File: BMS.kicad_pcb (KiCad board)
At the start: 4 copper layers, 44 x 71 mm, 129 parts, among them J1 12402012E212A, J3 Conn_01x02_Socket, J4 Conn_01x03_Pin, J5 Conn_01x10_Pin, J6 Conn_01x02_Pin, Q1 FZT853TA, Q2 PSMN020-100YS, Q3 PSMN020-100YS, Q4 PSMN3R7-100BSE, Q5 PSMN3R7-100BSE, SW1 SW_Push, SW2 SW_Push, U1 USBLC6-2SC6, U10 SQ1464EEH-T1_GE3, U11 MP2790DFP-0000-T, U12 TPS7B8133QDGNRQ1, U2 USBLC6-2SC6, U3 RP2350A, U5 SQ1464EEH-T1_GE3, U6 SQ1464EEH-T1_GE3, U7 SQ1464EEH-T1_GE3, U8 SQ1464EEH-T1_GE3, U9 SQ1464EEH-T1_GE3, X1 ABM8-272-T3

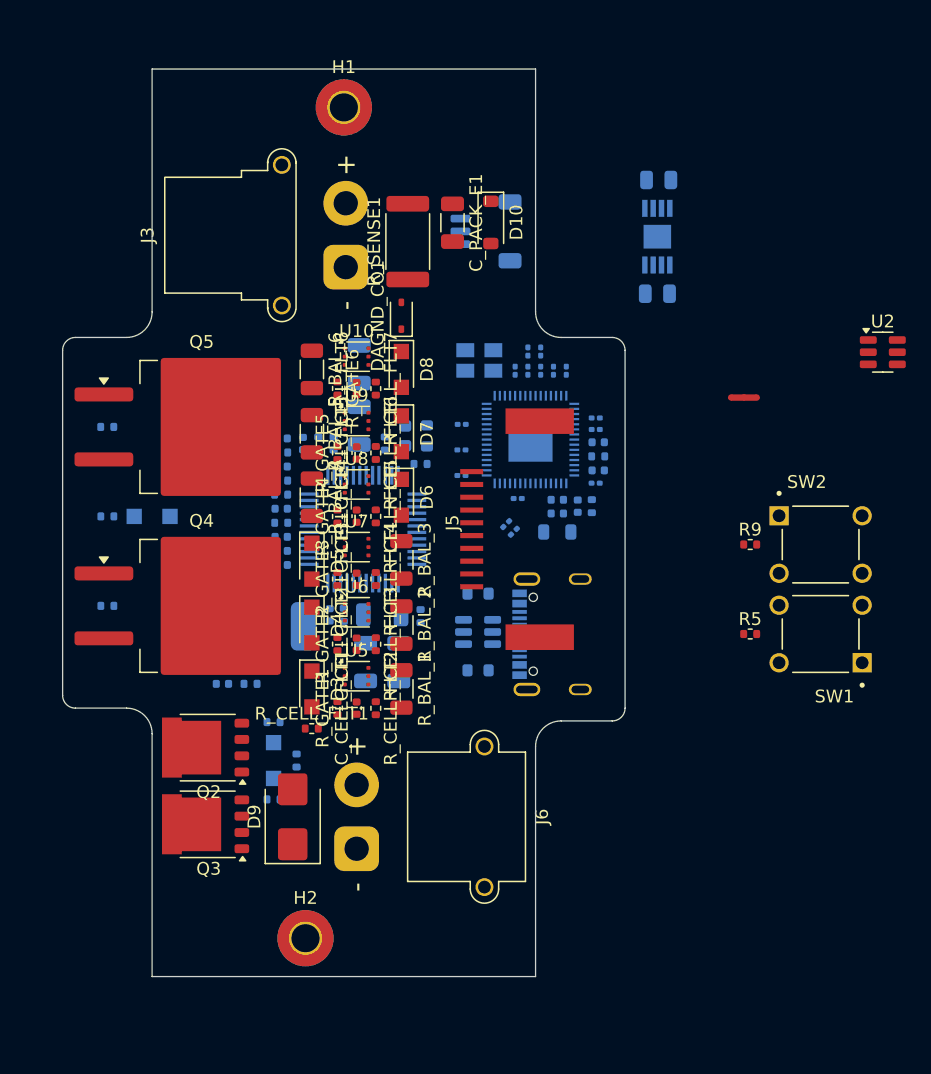
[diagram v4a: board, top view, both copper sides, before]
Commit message: Adding proper grounding
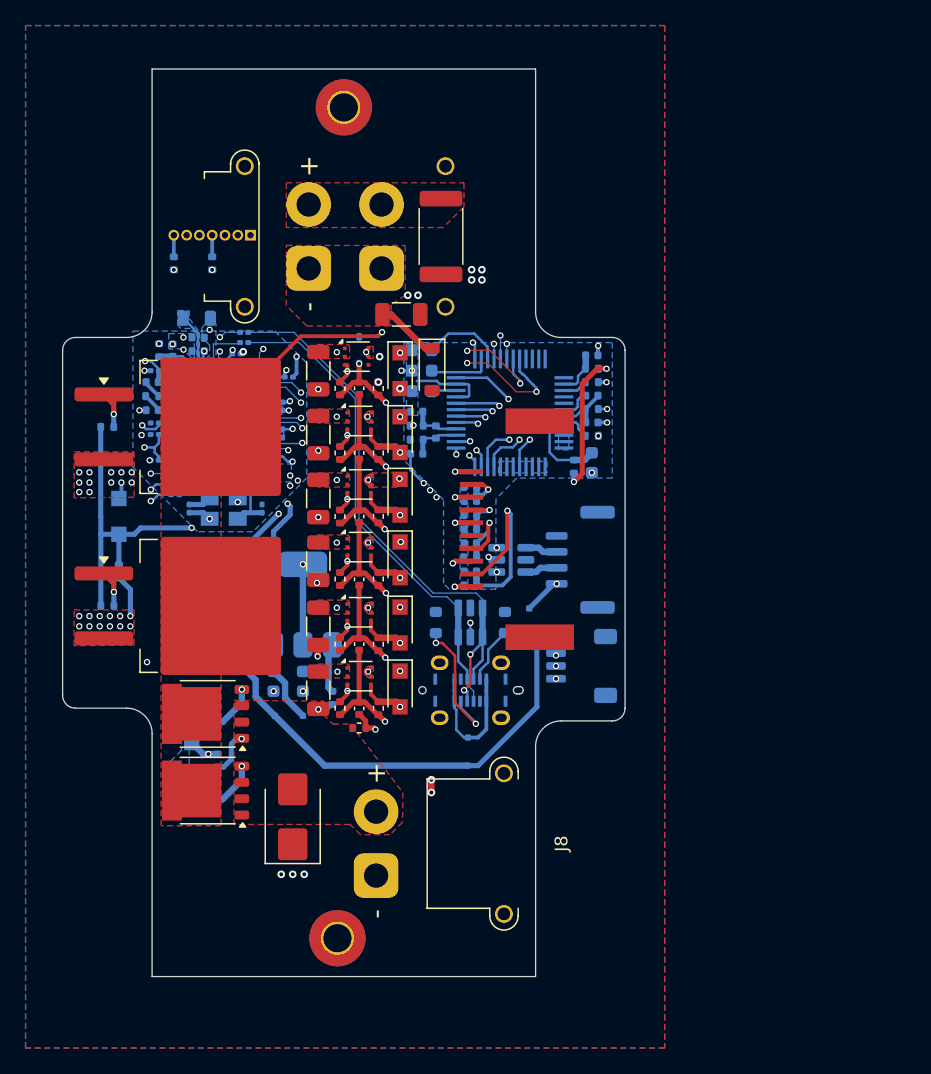
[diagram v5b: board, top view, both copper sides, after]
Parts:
- removed C4: 100n, Capacitor_SMD:C_0201_0603Metric
- removed C_3V1: 1 μF, Capacitor_SMD:C_0402_1005Metric
- removed the J4 at (161.0, 76.1)
- removed SW1, SW2: SW_Push, _BMS:SW_TS02-66-43-BK-160-LCR-D
- added C_3V3_1: 1 μF, Capacitor_SMD:C_0603_1608Metric, B.Cu at (156.0, 87.0)
- added D1: SS16HE, Diode_SMD:D_SOD-323F, B.Cu at (164.4, 106.7)
- added D11: SS16HE, Diode_SMD:D_SOD-323F, B.Cu at (159.6, 116.8)
- added D2: SS16HE, Diode_SMD:D_SOD-323F, B.Cu at (145.6, 114.0)
- added J2: Conn_01x04_Socket, Connector_JST:JST_GH_SM04B-GHS-TB_1x04-1MP_P1.25mm_Horizontal, B.Cu at (168.4, 101.8)
- added J3: Conn_01x02_Socket, Connector_AMASS:AMASS_XT30PW-F_1x02_P2.50mm_Horizontal, B.Cu at (152.8, 79.0)
- added J5: Conn_01x07_Socket, Connector_PinHeader_1.00mm:PinHeader_1x07_P1.00mm_Vertical, B.Cu at (142.6, 76.4)
- added J6: Conn_01x03_Pin, Connector_JST:JST_SH_SM03B-SRSS-TB_1x03-1MP_P1.00mm_Horizontal, B.Cu at (168.5, 110.1)
- C_CP1, C_MID1, C_SRN_GND1, C_SRN_SRP1, C_SRP_GND1: footprint Capacitor_SMD:C_1206_3216Metric -> Capacitor_SMD:C_0402_1005Metric
- C_REG1, C_VDD1, C_VREF1: footprint Capacitor_SMD:C_0402_1005Metric -> Capacitor_SMD:C_0603_1608Metric
- DAGND_CO1, R5, U2: moved to B.Cu
- J1: value 12402012E212A -> GSB1CA11101DSHR; footprint _BMS:AMPHENOL_12402012E212A -> _BMS:AMPHENOL_GSB1CA11101DSHR
- NT1: footprint NetTie:NetTie-3_SMD_Pad0.5mm -> NetTie:NetTie-2_SMD_Pad0.5mm
- R7: renamed from R9; moved to B.Cu
- R_MID1: footprint Resistor_SMD:R_0603_1608Metric -> Resistor_SMD:R_0402_1005Metric
- moved R5 53.6 mm to (136.6, 78.6), turned to -90 degrees
- moved C16 50.7 mm to (140.4, 109.6)
- moved R7 47.5 mm to (139.6, 78.6), turned to 90 degrees
- moved U4 44.5 mm to (140.6, 105.3), turned to 90 degrees
- moved C17 39.4 mm to (140.6, 101.0)
- moved NT1 39.0 mm to (156.8, 119.5), turned to 90 degrees
- moved R12 36.0 mm to (135.4, 85.4), turned to -90 degrees
- moved C10 35.6 mm to (135.1, 87.0), turned to 180 degrees
- moved R8 35.6 mm to (134.9, 87.9), turned to 180 degrees
- moved R9 35.2 mm to (134.9, 89.0), turned to 180 degrees
- moved C11 35.0 mm to (134.9, 90.1), turned to 180 degrees
- moved C12 34.5 mm to (135.1, 92.0), turned to 180 degrees
- moved C9 34.5 mm to (135.1, 91.1), turned to 180 degrees
- moved C13 34.0 mm to (136.5, 85.4), turned to 90 degrees
- moved U2 33.3 mm to (163.0, 101.8), turned to 180 degrees
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- renumbered C9 to C10, C22 to C16, C23 to C17, C10 to C9, J3 to J4, J5 to J7, J6 to J8, R7 to R8, R8 to R9, U12 to U4
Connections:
- net /main/microcontroller/SWCLK renamed /main/microcontroller/SWCLK_INT
- net /main/microcontroller/SWDIO renamed /main/microcontroller/SWDIO_INT
- C1 pad 1: GND -> GNDREF
- C10 pad 2: GND -> GNDREF
- C11 pad 2: GND -> GNDREF
- C12 pad 2: GND -> GNDREF
- C13 pad 2: GND -> GNDREF
- C14 pad 1: GND -> GNDREF
- C15 pad 1: GND -> GNDREF
- C2 pad 1: GND -> GNDREF
- C3 pad 1: GND -> GNDREF
- C5 pad 1: GND -> GNDREF
- C6 pad 2: GND -> GNDREF
- C7 pad 2: GND -> GNDREF
- C8 pad 2: GND -> GNDREF
- C9 pad 2: GND -> GNDREF
- C_REG1 pad 2: GNDREF -> GND
- C_SRN_GND1 pad 1: GNDREF -> /main/BMS/SRN
- C_SRN_GND1 pad 2: /main/BMS/SRN -> GNDREF
- C_SRP_GND1 pad 1: /main/BMS/SRP -> GNDREF
- C_SRP_GND1 pad 2: GNDREF -> /main/BMS/SRP
- C_VREF1 pad 1: GNDREF -> Net-(U11-VREF)
- C_VREF1 pad 2: Net-(U11-VREF) -> GNDREF
- J1 pad A6: Net-(J1-D+_A) -> /main/external_io/D+
- J1 pad A7: Net-(J1-D-_A) -> /main/external_io/D-
- R3 pad 1: Net-(J4-Pin_1) -> /main/external_io/SWCLK
- R4 pad 2: Net-(J4-Pin_3) -> /main/external_io/SWDIO
- R5 pad 1: GND -> /main/external_io/RUN
- R5 pad 2: Net-(R5-Pad2) -> Net-(U3-RUN)
- R7 pad 1: Net-(R9-Pad1) -> /main/microcontroller/QSPI_SS
- R7 pad 2: GND -> /main/external_io/BOOT
- R_MID1 pad 1: Net-(U11-VMID) -> /main/BMS/DRAIN
- R_MID1 pad 2: /main/BMS/DRAIN -> Net-(U11-VMID)
- U1 pad 1: Net-(J1-D+_A) -> /main/external_io/D+
- U1 pad 3: Net-(J1-D-_A) -> /main/external_io/D-
- U3 pad 10: unconnected-(U3-GPIO7-Pad10) -> /main/BMS/SCL
- U3 pad 12: unconnected-(U3-GPIO8-Pad12) -> GNDREF
- U3 pad 13: unconnected-(U3-GPIO9-Pad13) -> GNDREF
- U3 pad 17: unconnected-(U3-GPIO13-Pad17) -> GNDREF
- U3 pad 18: unconnected-(U3-GPIO14-Pad18) -> GNDREF
- U3 pad 19: unconnected-(U3-GPIO15-Pad19) -> GNDREF
- U3 pad 2: /main/BMS/SDA -> /main/external_io/TX
- U3 pad 20: unconnected-(U3-IOVDD-Pad20) -> GNDREF
- U3 pad 3: /main/BMS/SCL -> /main/external_io/RX
- U3 pad 47: GND -> GNDREF
- U3 pad 60: Net-(U3-QSPI_SS) -> /main/microcontroller/QSPI_SS
- U3 pad 61: GND -> GNDREF
- U3 pad 7: unconnected-(U3-GPIO4-Pad7) -> GNDREF
- U3 pad 8: unconnected-(U3-GPIO5-Pad8) -> GNDREF
- U3 pad 9: unconnected-(U3-GPIO6-Pad9) -> /main/BMS/SDA
- X1 pad 2: GND -> GNDREF
- X1 pad 4: GND -> GNDREF
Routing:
- net +3V3: track 0.00 -> 75.3 mm, vias 0 -> 8
- net Net-(D_CHG_VGS2-K): track 0.00 -> 62.3 mm, vias 0 -> 2
- net /main/BMS/TOP: track 0.00 -> 54.0 mm, vias 0 -> 4
- net Net-(D_CHG_VGS1-K): track 0.00 -> 50.2 mm, vias 0 -> 2
- net /main/BMS/SCL: track 0.00 -> 47.4 mm, vias 0 -> 4
- net /main/INT_5V: track 0.00 -> 45.9 mm, vias 0 -> 2
- net +1V1: track 0.00 -> 45.5 mm, vias 0 -> 3
- net /main/external_io/D+: track 0.00 -> 44.9 mm, vias 0 -> 2
- net /main/BMS/SDA: track 0.00 -> 42.9 mm, vias 0 -> 4
- net /main/external_io/SWCLK: track 0.00 -> 40.2 mm, vias 0 -> 2
- net /main/external_io/SWDIO: track 0.00 -> 40.1 mm, vias 0 -> 2
- net /main/BMS/CELL_5: track 0.00 -> 39.9 mm, vias 0 -> 2
- net /main/external_io/D-: track 0.00 -> 38.4 mm
- net /main/BMS/DRAIN: track 0.00 -> 37.4 mm, vias 0 -> 2
- net /main/housekeeping/5V_IN: track 0.00 -> 35.5 mm
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- added copper zone on B.Cu, net +1V1
- added copper zone on B.Cu, net /main/BMS/C10
- added copper zone on B.Cu, net /main/BMS/CELL_6
- added copper zone on F.Cu, net /main/BMS/DRAIN
- added copper zone on F.Cu, net /main/BMS/PACK+
- added copper zone on In1.Cu, net /main/BMS/PACK+
- added copper zone on F.Cu, net /main/BMS/PACK-
- added copper zone on F.Cu, net /main/BMS/TOP
- added copper zone on B.Cu, net /main/housekeeping/5V_IN
- added copper zone on B.Cu, net GND
- added copper zone on F.Cu, net GND
- added copper zone on In1.Cu, net GND
- added copper zone on In2.Cu, net GND
- added copper zone on In3.Cu, net GND
- added copper zone on In4.Cu, net GND
- added copper zone on B.Cu, net GNDREF
- added copper zone on In4.Cu, net GNDREF
- added copper zone on B.Cu, net Net-(D_CHG_VGS1-K)
- added copper zone on F.Cu, net Net-(R_BAL_1-Pad1)
- added copper zone on F.Cu, net Net-(R_BAL_2-Pad1)
- added copper zone on F.Cu, net Net-(R_BAL_3-Pad1)
- added copper zone on F.Cu, net Net-(R_BAL_4-Pad1)
- added copper zone on F.Cu, net Net-(R_BAL_5-Pad1)
- added copper zone on F.Cu, net Net-(R_BAL_6-Pad1)
- added copper zone on B.Cu, net Net-(U3-VREG_LX)
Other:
- copper layers 4 -> 6
- board text added: "-"

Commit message: Lots of changfes
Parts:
- removed the C20 at (159.8, 100.5)
- removed the J1 at (159.8, 112.0)
- removed NT1: NetTie_2, NetTie:NetTie-2_SMD_Pad0.5mm
- removed the R8 at (134.9, 87.9)
- removed the R9 at (134.9, 89.0)
- added C0: CELL0, _BMS:Harwin TP, F.Cu at (156.7, 87.4)
- added C1: CELL1, _BMS:Harwin TP, F.Cu at (156.4, 93.5)
- added C2: CELL2, _BMS:Harwin TP, F.Cu at (156.5, 98.4)
- added C22: 10n, Capacitor_SMD:C_0402_1005Metric, B.Cu at (159.8, 100.4)
- added C23: 10n, Capacitor_SMD:C_0402_1005Metric, B.Cu at (159.8, 102.7)
- added C3: CELL3, _BMS:Harwin TP, F.Cu at (156.5, 103.4)
- added C4: CELL4, _BMS:Harwin TP, F.Cu at (156.5, 108.4)
- added C4: 100n, Capacitor_SMD:C_0201_0603Metric, B.Cu at (144.2, 95.6)
- added C5: CELL5, _BMS:Harwin TP, F.Cu at (156.5, 110.9)
- added C5: 100n, Capacitor_SMD:C_0201_0603Metric, B.Cu at (138.8, 95.6)
- added C6: CELL6, _BMS:Harwin TP, F.Cu at (156.5, 114.1)
- added G***: LOGO, LOGO, F.Cu at (157.2, 131.5)
- added J6: 2169890001, _BMS:216989-0001_MOL, F.Cu at (138.6, 124.9)
- added R5: R, Resistor_SMD:R_0402_1005Metric, B.Cu at (163.6, 82.6)
- added R6: R, Resistor_SMD:R_0402_1005Metric, B.Cu at (162.5, 82.6)
- R_MID1, R_PACK_FLT1, R_TOP_FLT1: footprint Resistor_SMD:R_0402_1005Metric -> Resistor_SMD:R_0603_1608Metric
- R_REG1: footprint Resistor_SMD:R_0402_1005Metric -> Resistor_SMD:R_1206_3216Metric
- moved R2 29.3 mm to (142.9, 128.5), turned to 180 degrees
- moved R1 23.7 mm to (139.2, 122.2), turned to 0 degrees
- moved D1 21.9 mm to (145.6, 118.0), turned to 0 degrees
- moved U1 19.9 mm to (145.6, 120.7), turned to 180 degrees
- moved D3 14.0 mm to (145.6, 116.0), turned to 0 degrees
- moved C19 10.9 mm to (156.3, 89.1)
- moved D11 10.4 mm to (155.9, 76.5), turned to 90 degrees
- moved C_PACK_E1 7.24 mm to (158.3, 76.5), turned to 90 degrees
- moved R_SENSE1 3.90 mm to (161.4, 76.5)
- moved C21 3.30 mm to (159.8, 99.4)
- moved D10 2.02 mm to (147.8, 122.6)
- moved C_PACK_FLT1 1.76 mm to (167.7, 86.4), turned to 180 degrees
- moved R11 1.17 mm to (141.5, 83.8)
- moved R9 1.00 mm to (140.6, 78.6)
- moved R_PACK_FLT1 0.96 mm to (170.1, 86.4)
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- renumbered C9 to C10, C10 to C11, C11 to C12, C12 to C13, C13 to C14, C14 to C15, C15 to C16, C16 to C17, C17 to C18, C18 to C20, C5 to C6, C6 to C7, C7 to C8, C8 to C9, D9 to D10, D10 to D11, D11 to D3, D3 to D4, D4 to D5, D5 to D6, D6 to D7, D7 to D8, D8 to D9, J2 to J1, J3 to J2, J4 to J3, J5 to J4, J6 to J5, R5 to R7, R6 to R8, R7 to R9
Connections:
- net Net-(U3-USB_DM) renamed /main/microcontroller/D-
- net Net-(U3-USB_DP) renamed /main/microcontroller/D+
- C1 pad 1: GNDREF -> GND
- C10 pad 2: GNDREF -> GND
- C11 pad 2: GNDREF -> GND
- C12 pad 1: Net-(C11-Pad1) -> +3V3
- C12 pad 2: GNDREF -> GND
- C13 pad 2: GNDREF -> GND
- C14 pad 2: GNDREF -> GND
- C15 pad 1: GNDREF -> GND
- C16 pad 1: GNDREF -> GND
- C19 pad 1: GNDREF -> GND
- C19 pad 2: /main/BMS/NTC3 -> Net-(U11-NTCB)
- C2 pad 1: GNDREF -> GND
- C20 pad 1: GNDREF -> GND
- C21 pad 1: GNDREF -> GND
- C21 pad 2: /main/BMS/NTC1 -> /main/BMS/NTC3
- C3 pad 1: GNDREF -> GND
- C6 pad 1: GNDREF -> GND
- C7 pad 2: GNDREF -> GND
- C8 pad 2: GNDREF -> GND
- C9 pad 2: GNDREF -> GND
- C_3V3_1 pad 1: GNDREF -> GND
- C_MID1 pad 2: GNDREF -> GND
- C_PACK_E1 pad 2: GND -> /main/BMS/PACK-
- C_PACK_FLT1 pad 2: GNDREF -> GND
- C_REGIN1 pad 1: GNDREF -> GND
- C_SRN_GND1 pad 2: GNDREF -> GND
- C_SRP_GND1 pad 1: GNDREF -> GND
- C_TOP_FLT1 pad 2: GNDREF -> GND
- C_VDD1 pad 2: GNDREF -> GND
- C_VREF1 pad 2: GNDREF -> GND
- D11 pad 2: GND -> /main/BMS/PACK-
- D3 pad 2: VBUS_A -> /main/V_USB
- J4 pad 3: GND -> /main/external_io/BOOT
- J4 pad 4: /main/external_io/BOOT -> GND
- J4 pad 5: GND -> /main/BMS/NSHDN
- R13 pad 2: GNDREF -> Net-(U11-NTCB)
- R14 pad 2: GNDREF -> Net-(U11-NTCB)
- R15 pad 2: GNDREF -> Net-(U11-NTCB)
- R16 pad 2: GNDREF -> Net-(U11-NTCB)
- R_PACK_FLT1 pad 2: /main/BMS/TOP -> /main/BMS/PACK+
- U11 pad 21: GNDREF -> Net-(U11-NTCB)
- U11 pad 23: GNDREF -> GND
- U3 pad 12: GNDREF -> GND
- U3 pad 13: GNDREF -> GND
- U3 pad 17: GNDREF -> GND
- U3 pad 18: GNDREF -> GND
- U3 pad 19: GNDREF -> GND
- U3 pad 20: GNDREF -> +3V3
- U3 pad 44: /main/microcontroller/ADC_VREF -> +3V3
- U3 pad 47: GNDREF -> GND
- U3 pad 61: GNDREF -> GND
- U3 pad 7: GNDREF -> GND
- U3 pad 8: GNDREF -> GND
- X1 pad 2: GNDREF -> GND
- X1 pad 4: GNDREF -> GND
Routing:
- net /main/BMS/NSHDN: track 27.0 -> 62.2 mm
- net /main/EXT_5V: track 10.7 -> 39.7 mm, vias 2 -> 3
- net /main/V_USB: track 0.00 -> 26.5 mm, vias 0 -> 1
- net /main/housekeeping/5V_IN: track 35.5 -> 9.69 mm
- net Net-(U11-NTCB): track 0.00 -> 23.9 mm, vias 0 -> 2
- net /main/external_io/D-: track 38.4 -> 61.6 mm
- net GNDREF: track 16.5 -> 0.00 mm, vias 25 -> 0
- net /main/BMS/PACK+: track 9.67 -> 25.9 mm, vias 24 -> 25
- net /main/external_io/D+: track 44.9 -> 59.4 mm, vias 2 -> 0
- net /main/BMS/TOP: track 54.0 -> 42.5 mm, vias 4 -> 3
- net VBUS_A: track 10.8 -> 0.00 mm
- net Net-(J6-CC1): track 10.9 -> 2.86 mm, vias 2 -> 0
- net GND: track 6.03 -> 13.2 mm, vias 17 -> 71
- net +3V3: track 75.3 -> 81.9 mm
- net /main/BMS/CELL_5: track 39.9 -> 45.1 mm
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- added copper zone on B.Cu, net +3V3
- removed copper zone on B.Cu, net GNDREF
- removed copper zone on In4.Cu, net GNDREF
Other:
- board size 44 x 71 mm -> 44 x 69 mm
- board text added: "Alejandro A."
- board text added: "Ezzat S."

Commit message: Tweaks and production files
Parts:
- removed the J6 at (138.6, 124.9)
- removed the R2 at (142.9, 128.5)
- added J1: UJ20-C-H-G-SMT-1-P16-TR, _BMS:SAMESKY_UJ20-C-H-G-SMT-1-P16-TR, B.Cu at (135.7, 127.8)
- added J9: Conn_01x02_Socket, Connector_JST:JST_PH_B2B-PH-K_1x02_P2.00mm_Vertical, F.Cu at (2.48, 2.23)
- added R1: 5.1k, Resistor_SMD:R_0603_1608Metric, B.Cu at (144.8, 120.8)
- C_PACK_E1, D11, R_SENSE1: moved to B.Cu
- R5, R6: value R -> 33k
- moved G*** 18.4 mm to (139.0, 128.8)
- moved R2 10.4 mm to (145.9, 130.2), turned to 90 degrees
- moved U2 4.81 mm to (145.9, 125.5), turned to -90 degrees
- moved R_SENSE1 0.25 mm to (161.7, 76.5)
- moved D11 0.15 mm to (156.1, 76.5)
- moved C_PACK_E1 0.15 mm to (158.4, 76.5)
- renumbered J1 to J2, J2 to J3, J3 to J4, J4 to J5, J5 to J6, R1 to R2, U2 to U1, U1 to U2
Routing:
- net /main/BMS/NSHDN: track 62.2 -> 53.9 mm
- net /main/BMS/PACK-: track 20.9 -> 27.0 mm
- net Net-(J1-CC2): track 0.00 -> 5.63 mm
- net /main/V_USB: track 26.5 -> 23.0 mm, vias 1 -> 0
- net Net-(J6-CC2): track 2.92 -> 0.00 mm
- net /main/external_io/D+: track 59.4 -> 60.6 mm
- net /main/external_io/D-: track 61.6 -> 62.6 mm
- net GND: track 13.2 -> 12.6 mm, vias 71 -> 67
- added copper zone on B.Cu, net /main/BMS/PACK+
- added copper zone on B.Cu, net /main/BMS/PACK-
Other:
- board text removed: "-"
